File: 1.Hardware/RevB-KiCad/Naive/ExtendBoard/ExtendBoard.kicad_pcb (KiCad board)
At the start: 2 copper layers, 29.4 x 26.2 mm, 11 parts, among them CON1 FH12-8S-0.5SH(55), Q1 AO3400A, U1 AL5802

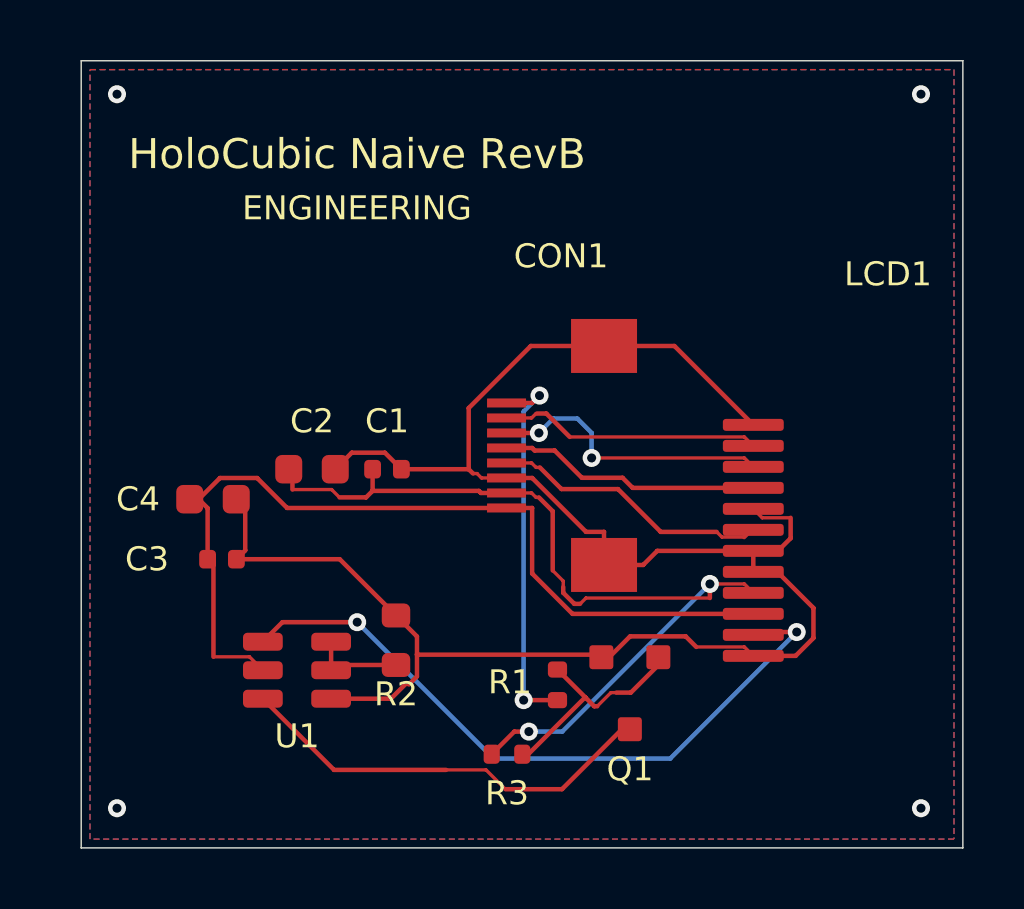
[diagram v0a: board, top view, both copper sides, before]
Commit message: Resolve Naive display landing and fabrication rules; add bring-up tools
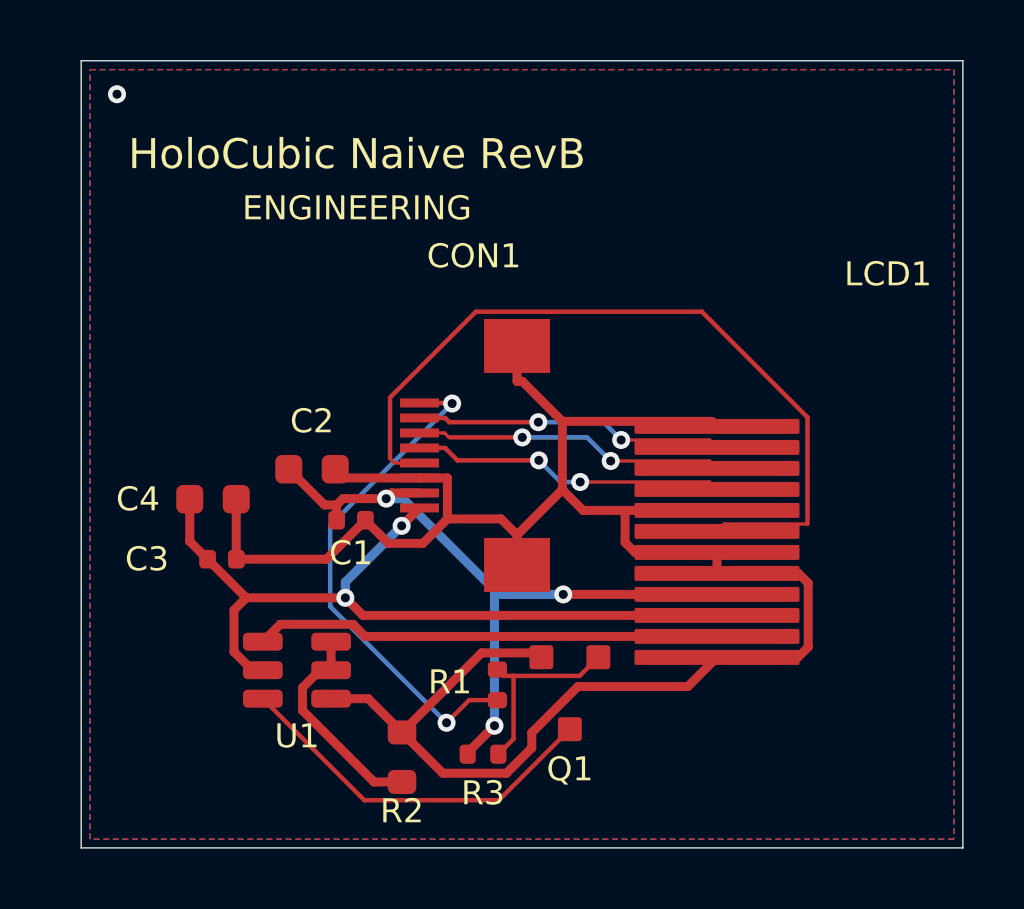
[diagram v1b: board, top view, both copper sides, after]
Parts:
- moved R2 3.91 mm to (144.5, 115.1)
- moved CON1 2.90 mm to (146.9, 105.0)
- moved C1 2.08 mm to (142.8, 107.2)
- moved Q1 2.00 mm to (150.1, 113.0)
- moved R1 2.00 mm to (147.7, 112.7)
- moved R3 0.80 mm to (147.2, 115.0)
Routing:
- net DC: track 9.35 -> 26.3 mm
- net LED_K: track 23.2 -> 15.5 mm, vias 2 -> 0
- net GND: track 65.7 -> 72.4 mm, vias 4 -> 1
- net 3V3: track 30.3 -> 23.7 mm, vias 2 -> 3
- net LCD_BL: track 12.7 -> 17.0 mm
- net BL_SENSE: track 3.18 -> 7.21 mm
- net VDD_5V: track 29.2 -> 27.2 mm, vias 0 -> 2
- net BL_EN: track 14.4 -> 12.6 mm
- net SCK: track 8.78 -> 10.5 mm, vias 0 -> 2
- net RES: track 8.73 -> 10.3 mm, vias 0 -> 2
- net MOSI: track 9.58 -> 10.4 mm
- net BL_GATE: track 7.32 -> 6.53 mm
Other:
- rule pad_to_mask_clearance: 0.0762 -> 0.025
